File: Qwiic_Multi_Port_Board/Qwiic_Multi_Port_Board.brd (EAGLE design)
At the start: 25.4 x 25.4 mm, 10 parts, among them J1 QWIIC_RIGHT_ANGLE, J2 QWIIC_RIGHT_ANGLE, J3 QWIIC_RIGHT_ANGLE, J4 QWIIC_RIGHT_ANGLE

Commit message: Finishing touches
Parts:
- added H1, H2: STAND-OFFTIGHT, SparkFun-Hardware:STAND-OFF-TIGHT
- added U$10: (no value), SparkX:SPARKX-SMALL
- added U$7: (no value), buzzard_labels (75):MULTI1
- added U$8: (no value), buzzard_labels (75):PORT2
- added U$9: (no value), buzzard_labels (75):BOARD3
- U$1: device SparkFun-Aesthetics:QWIIC_8MM -> SparkFun-Aesthetics:QWIIC_6MM
- U$3: device buzzard_labels (75):QWIIC0 -> SparkFun-Aesthetics:QWIIC_6MM
- moved U$2 15.8 mm to (12.7, 9.40)
- moved U$1 15.1 mm to (12.7, 16.0)
- moved U$3 3.07 mm to (12.6, 16.0), flipped to the bottom
- moved U$4 0.80 mm to (8.13, 13.5)
- moved J3 0.76 mm to (20.3, 12.7)
- moved J4 0.76 mm to (12.7, 20.3)
- moved J1 0.76 mm to (12.7, 5.08)
- moved J2 0.76 mm to (5.08, 12.7)
- moved U$5 0.64 mm to (12.4, 13.3)
- moved U$6 0.63 mm to (9.65, 11.7)
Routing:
- net 3.3V: track 35.6 -> 38.6 mm
- net SCL: track 41.8 -> 44.2 mm
- net SDA: track 34.7 -> 36.4 mm
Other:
- outline, holes or cut-outs redrawn

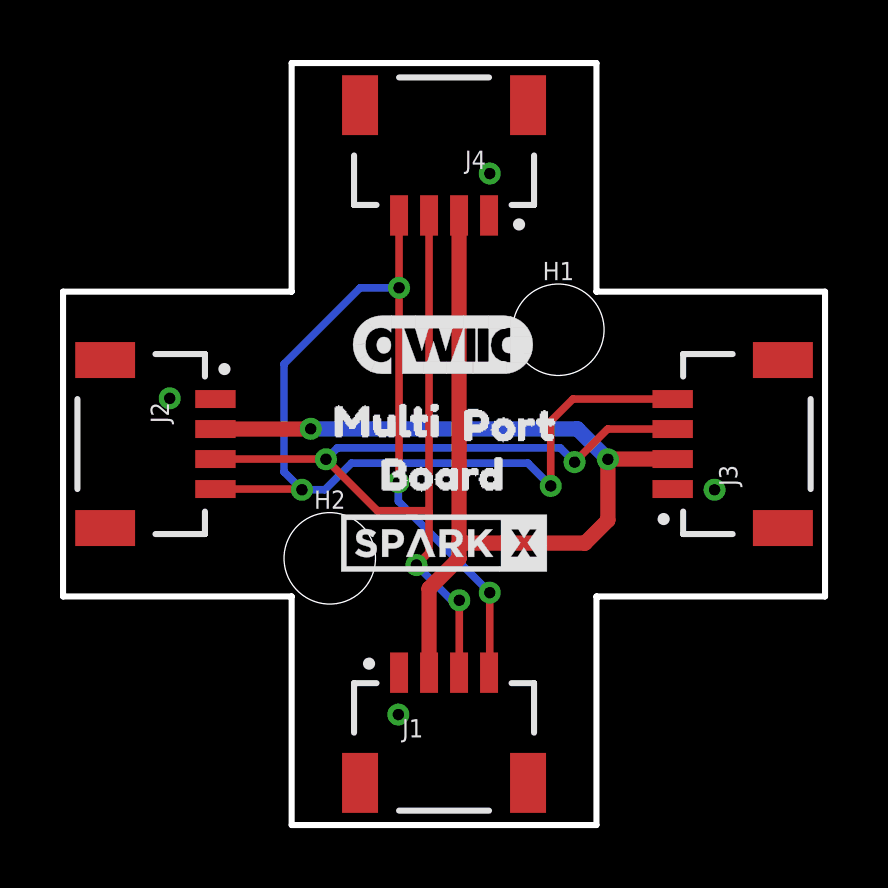
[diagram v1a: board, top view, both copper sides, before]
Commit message: Decrease plus width. Move silk. Change to letter frame.
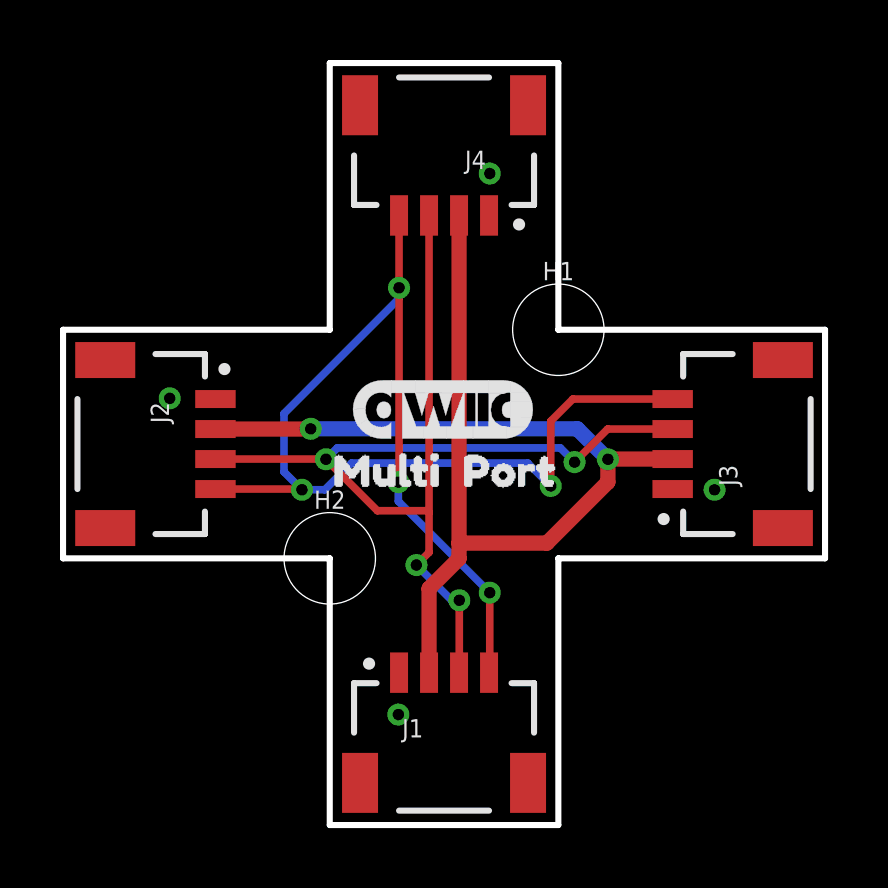
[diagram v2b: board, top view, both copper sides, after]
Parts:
- removed U$10: (no value), SparkX:SPARKX-SMALL
- removed U$6, U$9: (no value), buzzard_labels (75):BOARD3
- added FRAME1: FRAME-LETTER, SparkFun-Aesthetics:CREATIVE_COMMONS
- moved U$2 3.81 mm to (12.7, 5.59), flipped to the bottom
- moved U$3 2.16 mm to (12.7, 13.8)
- moved U$1 2.16 mm to (12.7, 13.8)
- moved U$4 1.65 mm to (8.13, 11.8)
- moved U$7 1.53 mm to (17.4, 11.8)
- moved U$5 1.52 mm to (12.4, 11.8)
- moved U$8 1.52 mm to (13.0, 11.8)
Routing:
- net SCL: track 44.2 -> 43.5 mm
- net 3.3V: track 38.6 -> 37.9 mm
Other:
- outline, holes or cut-outs redrawn
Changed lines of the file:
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@@
 <?xml version="1.0" encoding="utf-8"?>
 <!DOCTYPE eagle SYSTEM "eagle.dtd">
-<eagle version="9.4.2">
+<eagle version="9.6.2">
 <drawing>
 <settings>
@@
 <layer number="1" name="Top" color="4" fill="1" visible="yes" active="yes"/>
 <layer number="2" name="Route2" color="16" fill="1" visible="no" active="no"/>
+<layer number="3" name="Route3" color="4" fill="3" visible="no" active="no"/>
+<layer number="4" name="Route4" color="1" fill="4" visible="no" active="no"/>
+<layer number="5" name="Route5" color="4" fill="4" visible="no" active="no"/>
+<layer number="6" name="Route6" color="1" fill="8" visible="no" active="no"/>
+<layer number="7" name="Route7" color="4" fill="8" visible="no" active="no"/>
+<layer number="8" name="Route8" color="1" fill="2" visible="no" active="no"/>
+<layer number="9" name="Route9" color="4" fill="2" visible="no" active="no"/>
+<layer number="10" name="Route10" color="1" fill="7" visible="no" active="no"/>
+<layer number="11" name="Route11" color="4" fill="7" visible="no" active="no"/>
+<layer number="12" name="Route12" color="1" fill="5" visible="no" active="no"/>
+<layer number="13" name="Route13" color="4" fill="5" visible="no" active="no"/>
+<layer number="14" name="Route14" color="1" fill="6" visible="no" active="no"/>
 <layer number="15" name="Route15" color="23" fill="1" visible="no" active="no"/>
 <layer number="16" name="Bottom" color="1" fill="1" visible="yes" active="yes"/>
@@
 <board>
 <plain>
-<wire x1="7.62" y1="0" x2="17.78" y2="0" width="0.2032" layer="20"/>
-<wire x1="25.4" y1="7.62" x2="25.4" y2="17.78" width="0.2032" layer="20"/>
-<wire x1="17.78" y1="25.4" x2="7.62" y2="25.4" width="0.2032" layer="20"/>
-<wire x1="0" y1="17.78" x2="0" y2="7.62" width="0.2032" layer="20"/>
-<wire x1="7.62" y1="0" x2="7.62" y2="7.62" width="0.2032" layer="20"/>
-<wire x1="7.62" y1="7.62" x2="0" y2="7.62" width="0.2032" layer="20"/>
-<wire x1="17.78" y1="0" x2="17.78" y2="7.62" width="0.2032" layer="20"/>
-<wire x1="17.78" y1="7.62" x2="25.4" y2="7.62" width="0.2032" layer="20"/>
-<wire x1="17.78" y1="25.4" x2="17.78" y2="17.78" width="0.2032" layer="20"/>
-<wire x1="17.78" y1="17.78" x2="25.4" y2="17.78" width="0.2032" layer="20"/>
-<wire x1="7.62" y1="25.4" x2="7.62" y2="17.78" width="0.2032" layer="20"/>
-<wire x1="7.62" y1="17.78" x2="0" y2="17.78" width="0.2032" layer="20"/>
+<wire x1="8.89" y1="0" x2="16.51" y2="0" width="0.2032" layer="20"/>
+<wire x1="25.4" y1="8.89" x2="25.4" y2="16.51" width="0.2032" layer="20"/>
+<wire x1="16.51" y1="25.4" x2="8.89" y2="25.4" width="0.2032" layer="20"/>
+<wire x1="0" y1="16.51" x2="0" y2="8.89" width="0.2032" layer="20"/>
+<wire x1="8.89" y1="0" x2="8.89" y2="8.89" width="0.2032" layer="20"/>
+<wire x1="8.89" y1="8.89" x2="0" y2="8.89" width="0.2032" layer="20"/>
+<wire x1="16.51" y1="0" x2="16.51" y2="8.89" width="0.2032" layer="20"/>
+<wire x1="16.51" y1="8.89" x2="25.4" y2="8.89" width="0.2032" layer="20"/>
+<wire x1="16.51" y1="25.4" x2="16.51" y2="16.51" width="0.2032" layer="20"/>
+<wire x1="16.51" y1="16.51" x2="25.4" y2="16.51" width="0.2032" layer="20"/>
+<wire x1="8.89" y1="25.4" x2="8.89" y2="16.51" width="0.2032" layer="20"/>
+<wire x1="8.89" y1="16.51" x2="0" y2="16.51" width="0.2032" layer="20"/>
 </plain>
 <attributes>
@@
 <attribute name="VALUE" x="14.351" y="23.622" size="0.6096" layer="27" font="vector" ratio="20" rot="R180"/>
 </element>
-<element name="U$2" library="SparkX" package="SPARKX-SMALL" value="" x="12.7" y="9.398" smashed="yes"/>
-<element name="U$4" library="buzzard_labels (75)" package="MULTI1" value="" x="8.128" y="13.462" smashed="yes"/>
-<element name="U$5" library="buzzard_labels (75)" package="PORT2" value="" x="12.446" y="13.335" smashed="yes"/>
-<element name="U$6" library="buzzard_labels (75)" package="BOARD3" value="" x="9.652" y="11.684" smashed="yes"/>
-<element name="U$1" library="SparkFun-Aesthetics" package="QWIIC_6MM" value="" x="12.7" y="16.002" smashed="yes"/>
-<element name="U$3" library="SparkFun-Aesthetics" package="QWIIC_6MM" value="" x="12.573" y="16.002" smashed="yes" rot="MR0"/>
-<element name="U$7" library="buzzard_labels (75)" package="MULTI1" value="" x="17.272" y="13.335" smashed="yes" rot="MR0"/>
-<element name="U$8" library="buzzard_labels (75)" package="PORT2" value="" x="12.954" y="13.335" smashed="yes" rot="MR0"/>
-<element name="U$9" library="buzzard_labels (75)" package="BOARD3" value="" x="15.621" y="11.684" smashed="yes" rot="MR0"/>
-<element name="U$10" library="SparkX" package="SPARKX-SMALL" value="" x="12.7" y="9.398" smashed="yes" rot="MR0"/>
+<element name="U$2" library="SparkX" package="SPARKX-SMALL" value="" x="12.7" y="5.588" smashed="yes" rot="MR0"/>
+<element name="U$4" library="buzzard_labels (75)" package="MULTI1" value="" x="8.128" y="11.811" smashed="yes"/>
+<element name="U$5" library="buzzard_labels (75)" package="PORT2" value="" x="12.446" y="11.811" smashed="yes"/>
+<element name="U$1" library="SparkFun-Aesthetics" package="QWIIC_6MM" value="" x="12.7" y="13.843" smashed="yes"/>
+<element name="U$3" library="SparkFun-Aesthetics" package="QWIIC_6MM" value="" x="12.7" y="13.843" smashed="yes" rot="MR0"/>
+<element name="U$7" library="buzzard_labels (75)" package="MULTI1" value="" x="17.399" y="11.811" smashed="yes" rot="MR0"/>
+<element name="U$8" library="buzzard_labels (75)" package="PORT2" value="" x="12.954" y="11.811" smashed="yes" rot="MR0"/>
 <element name="H1" library="SparkFun-Hardware" package="STAND-OFF-TIGHT" value="STAND-OFFTIGHT" x="16.51" y="16.51" smashed="yes">
 <attribute name="NAME" x="16.51" y="18.161" size="0.6096" layer="25" font="vector" ratio="20" align="bottom-center"/>
@@
 <attribute name="NAME" x="8.89" y="10.541" size="0.6096" layer="25" font="vector" ratio="20" align="bottom-center"/>
 <attribute name="VALUE" x="8.89" y="7.239" size="0.6096" layer="27" font="vector" ratio="20" align="top-center"/>
+</element>
+<element name="FRAME1" library="SparkFun-Aesthetics" package="CREATIVE_COMMONS" value="FRAME-LETTER" x="21.59" y="-8.89" smashed="yes">
+<attribute name="DESIGNER" value="" x="21.59" y="-8.89" size="1.778" layer="27" display="off"/>
+<attribute name="REV" value="" x="21.59" y="-8.89" size="1.778" layer="27" display="off"/>
 </element>
 </elements>
@@
 <wire x1="14.2" y1="5.08" x2="14.224" y2="5.104" width="0.254" layer="1"/>
 <wire x1="7.9629" y1="11.176" x2="7.366" y2="11.7729" width="0.254" layer="16"/>
-<wire x1="7.366" y1="15.367" x2="9.906" y2="17.907" width="0.254" layer="16"/>
-<wire x1="9.906" y1="17.907" x2="11.2" y2="17.907" width="0.254" layer="16"/>
+<wire x1="11.2" y1="17.907" x2="11.2" y2="17.55" width="0.254" layer="16"/>
+<wire x1="11.2" y1="17.55" x2="7.366" y2="13.716" width="0.254" layer="16"/>
 <via x="11.2" y="17.907" extent="1-16" drill="0.381"/>
-<wire x1="7.366" y1="11.7729" x2="7.366" y2="15.367" width="0.254" layer="16"/>
+<wire x1="7.366" y1="11.7729" x2="7.366" y2="13.716" width="0.254" layer="16"/>
 <wire x1="5.08" y1="11.2" x2="7.9389" y2="11.2" width="0.254" layer="1"/>
 <wire x1="7.9389" y1="11.2" x2="7.9629" y2="11.176" width="0.254" layer="1"/>
@@
 <via x="21.717" y="11.176" extent="1-16" drill="0.381"/>
 <polygon width="0.2032" layer="1" isolate="0.3048">
-<vertex x="0" y="17.78"/>
-<vertex x="0" y="7.62"/>
-<vertex x="7.62" y="7.62"/>
-<vertex x="7.62" y="0"/>
-<vertex x="17.78" y="0"/>
-<vertex x="17.78" y="7.62"/>
-<vertex x="25.4" y="7.62"/>
-<vertex x="25.4" y="17.78"/>
-<vertex x="17.78" y="17.78"/>
-<vertex x="17.78" y="25.4"/>
-<vertex x="7.62" y="25.4"/>
-<vertex x="7.62" y="17.78"/>
+<vertex x="0" y="16.51"/>
+<vertex x="0" y="8.89"/>
+<vertex x="8.89" y="8.89"/>
+<vertex x="8.89" y="0"/>
+<vertex x="16.51" y="0"/>
+<vertex x="16.51" y="8.89"/>
+<vertex x="25.4" y="8.89"/>
+<vertex x="25.4" y="16.51"/>
+<vertex x="16.51" y="16.51"/>
+<vertex x="16.51" y="25.4"/>
+<vertex x="8.89" y="25.4"/>
+<vertex x="8.89" y="16.51"/>
 </polygon>
 <polygon width="0.2032" layer="16" isolate="0.3048">
-<vertex x="0" y="17.78"/>
-<vertex x="0" y="7.62"/>
-<vertex x="7.62" y="7.62"/>
-<vertex x="7.62" y="0"/>
-<vertex x="17.78" y="0"/>
-<vertex x="17.78" y="7.62"/>
-<vertex x="25.4" y="7.62"/>
-<vertex x="25.4" y="17.78"/>
-<vertex x="17.78" y="17.78"/>
-<vertex x="17.78" y="25.4"/>
-<vertex x="7.62" y="25.4"/>
-<vertex x="7.62" y="17.78"/>
+<vertex x="0" y="16.51"/>
+<vertex x="0" y="8.89"/>
+<vertex x="8.89" y="8.89"/>
+<vertex x="8.89" y="0"/>
+<vertex x="16.51" y="0"/>
+<vertex x="16.51" y="8.89"/>
+<vertex x="25.4" y="8.89"/>
+<vertex x="25.4" y="16.51"/>
+<vertex x="16.51" y="16.51"/>
+<vertex x="16.51" y="25.4"/>
+<vertex x="8.89" y="25.4"/>
+<vertex x="8.89" y="16.51"/>
 </polygon>
 </signal>
@@
 <wire x1="17.145" y1="13.208" x2="18.161" y2="12.192" width="0.508" layer="16"/>
 <via x="18.161" y="12.192" extent="1-16" drill="0.381"/>
-<wire x1="18.161" y1="12.192" x2="18.161" y2="10.16" width="0.508" layer="1"/>
-<wire x1="18.161" y1="10.16" x2="17.399" y2="9.398" width="0.508" layer="1"/>
+<wire x1="18.161" y1="12.192" x2="18.161" y2="11.43" width="0.508" layer="1"/>
+<wire x1="18.161" y1="11.43" x2="16.129" y2="9.398" width="0.508" layer="1"/>
 <wire x1="5.08" y1="13.2" x2="8.247" y2="13.2" width="0.508" layer="1"/>
 <wire x1="8.247" y1="13.2" x2="8.255" y2="13.208" width="0.254" layer="1"/>
 <wire x1="13.2" y1="20.32" x2="13.2" y2="9.398" width="0.508" layer="1"/>
 <wire x1="13.2" y1="8.882" x2="13.2" y2="9.398" width="0.508" layer="1"/>
-<wire x1="17.399" y1="9.398" x2="13.2" y2="9.398" width="0.508" layer="1"/>
+<wire x1="16.129" y1="9.398" x2="13.2" y2="9.398" width="0.508" layer="1"/>
 <wire x1="20.32" y1="12.2" x2="18.169" y2="12.2" width="0.508" layer="1"/>
 <wire x1="18.169" y1="12.2" x2="18.161" y2="12.192" width="0.254" layer="1"/>
